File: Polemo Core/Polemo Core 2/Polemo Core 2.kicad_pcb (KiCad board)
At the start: 4 copper layers, 40 x 100 mm, 174 parts, among them P1 Header-Male-2.54_2x2, P2 Header-Male-2.54_2x2, Q1 BC847_C2910145, Q2 MMBT5551LT1G, Q3 AO3401A, Q4 AO3401A, Q5 MMBT5551LT1G, U1 ATSAML21G18B-AUT, U10 74LVC1G08GV,125, U11 LT3014BHVES5#TRMPBF, U12 TXU0202DCUR, U13 TLV7031DBVR, U14 TLR341G-GTR, U15 803-87-006-10-001101, U2 XC6209F332MR-G, U3 MC14043BDR2G, U4 LMV793MFX/NOPB, U5 TPS7A2030PDBVR, U6 TLV3201AIDBVT, U7 OPA357AIDBVR, U8 TLR341G-GTR, U9 MF-ASML020/6-2, X1 32.768kHz

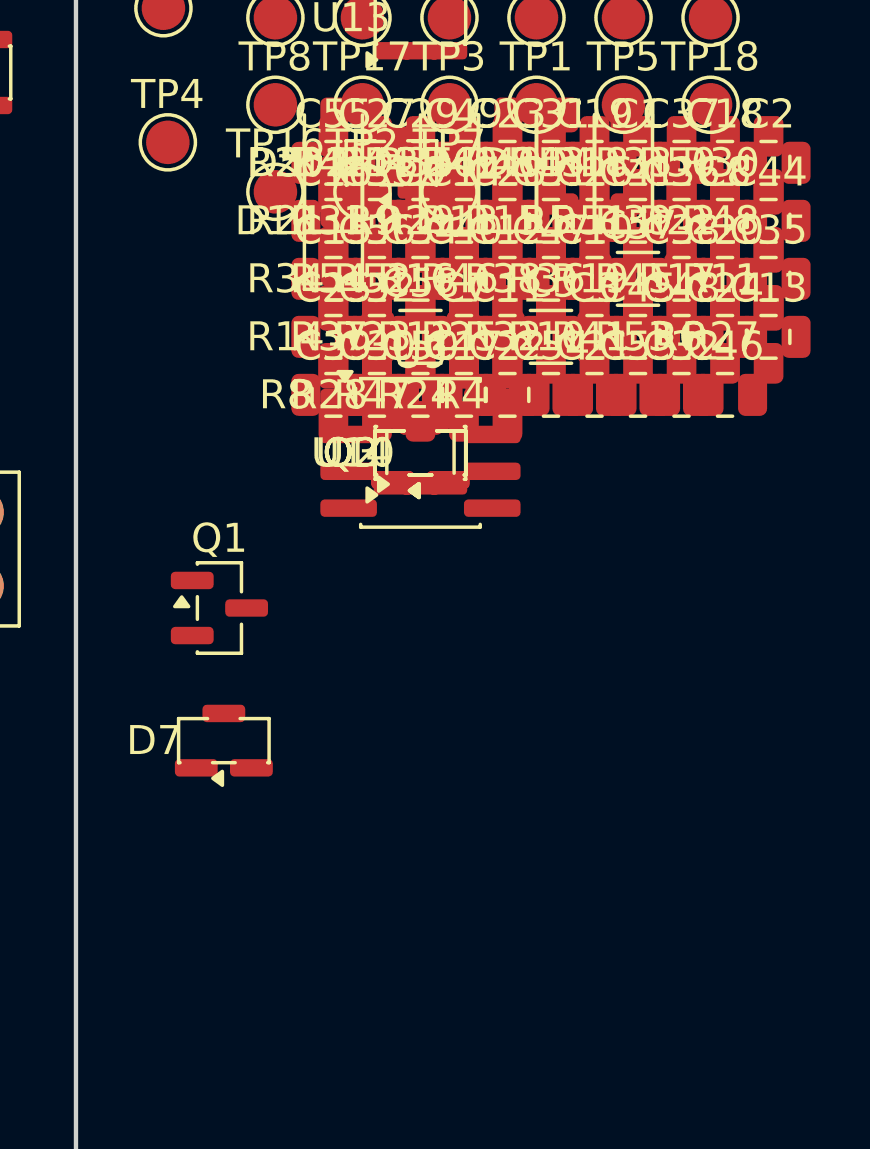
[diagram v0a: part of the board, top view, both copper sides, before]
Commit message: Moved some components
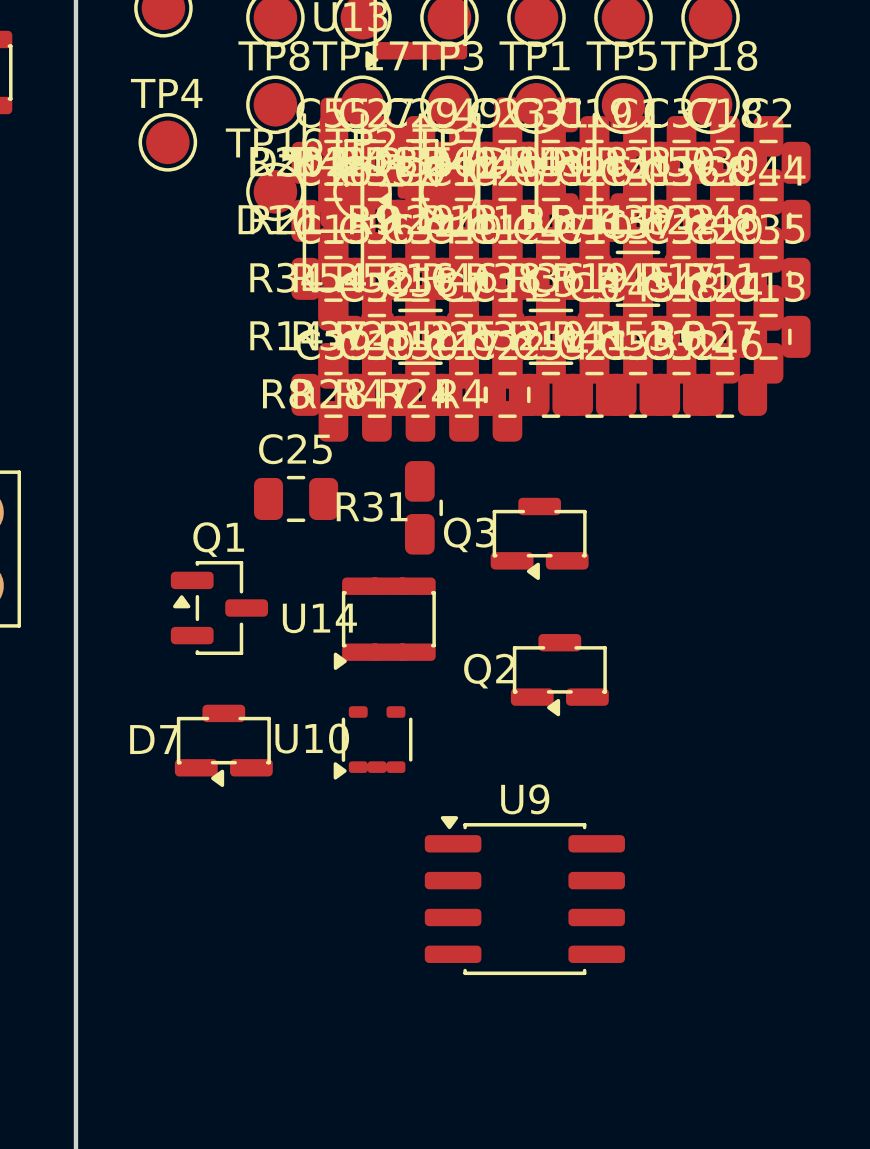
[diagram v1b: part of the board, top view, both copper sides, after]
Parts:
- moved U9 15.8 mm to (105.5, 131.9)
- moved R31 10.0 mm to (101.9, 118.4)
- moved U10 10.00 mm to (100.4, 126.4)
- moved Q2 8.89 mm to (106.7, 124.0)
- moved U14 5.84 mm to (100.8, 122.2)
- moved C25 5.73 mm to (97.6, 118.1)
- moved Q3 4.96 mm to (106.0, 119.3)
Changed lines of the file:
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@@
 	(footprint "Package_TO_SOT_SMD:SOT-23-6"
 		(layer "F.Cu")
-		(at 101.8752 116.4712 90)
+		(at 100.7872 122.2049 90)
 		(descr "SOT, 6 Pin (JEDEC MO-178 Var AB https://www.jedec.org/document_search?search_api_views_fulltext=MO-178), generated with kicad-footprint-generator ipc_gullwing_generator.py")
 		(tags "SOT TO_SOT_SMD")
@@
 	(footprint "Resistor_SMD:R_0805_2012Metric"
 		(layer "F.Cu")
-		(at 100.3752 108.4712 90)
+		(at 101.854 118.3659 90)
 		(descr "Resistor SMD 0805 (2012 Metric), square (rectangular) end terminal, IPC-7351 nominal, (Body size source: IPC-SM-782 page 72, https://www.pcb-3d.com/wordpress/wp-content/uploads/ipc-sm-782a_amendment_1_and_2.pdf), generated with kicad-footprint-generator")
 		(tags "resistor")
@@
 	(footprint "Package_TO_SOT_SMD:SOT-23"
 		(layer "F.Cu")
-		(at 101.8752 116.4712 90)
+		(at 105.984 119.2553 90)
 		(descr "SOT, 3 Pin (JEDEC TO-236 Var AB https://www.jedec.org/document_search?search_api_views_fulltext=TO-236), generated with kicad-footprint-generator ipc_gullwing_generator.py")
 		(tags "SOT TO_SOT_SMD")
@@
 	(footprint "Package_SO:SOIC-8_3.9x4.9mm_P1.27mm"
 		(layer "F.Cu")
-		(at 101.8752 116.4712)
+		(at 105.475 131.8514)
 		(descr "SOIC, 8 Pin (JEDEC MS-012AA, https://www.analog.com/media/en/package-pcb-resources/package/pkg_pdf/soic_narrow-r/r_8.pdf), generated with kicad-footprint-generator ipc_gullwing_generator.py")
 		(tags "SOIC SO")
@@
 	(footprint "Capacitor_SMD:C_0805_2012Metric"
 		(layer "F.Cu")
-		(at 98.8752 112.4712)
+		(at 97.5868 118.0592)
 		(descr "Capacitor SMD 0805 (2012 Metric), square (rectangular) end terminal, IPC-7351 nominal, (Body size source: IPC-SM-782 page 76, https://www.pcb-3d.com/wordpress/wp-content/uploads/ipc-sm-782a_amendment_1_and_2.pdf, https://docs.google.com/spreadsheets/d/1BsfQQcO9C6DZCsRaXUlFlo91Tg2WpOkGARC1WS5S8t0/edit?usp=sharing), generated with kicad-footprint-generator")
 		(tags "capacitor")
@@
 	(footprint "Package_TO_SOT_SMD:SOT-23"
 		(layer "F.Cu")
-		(at 101.8752 116.4712 90)
+		(at 106.68 123.952 90)
 		(descr "SOT, 3 Pin (JEDEC TO-236 Var AB https://www.jedec.org/document_search?search_api_views_fulltext=TO-236), generated with kicad-footprint-generator ipc_gullwing_generator.py")
 		(tags "SOT TO_SOT_SMD")
@@
 	(footprint "Package_TO_SOT_SMD:SOT-353_SC-70-5"
 		(layer "F.Cu")
-		(at 101.8752 116.4712 90)
+		(at 100.3808 126.3548 90)
 		(descr "SOT-353, SC-70-5")
 		(tags "SOT-353 SC-70-5")
